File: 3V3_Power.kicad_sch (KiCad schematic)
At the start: 5 parts, among them U5 AP2127N-3.3TRG1

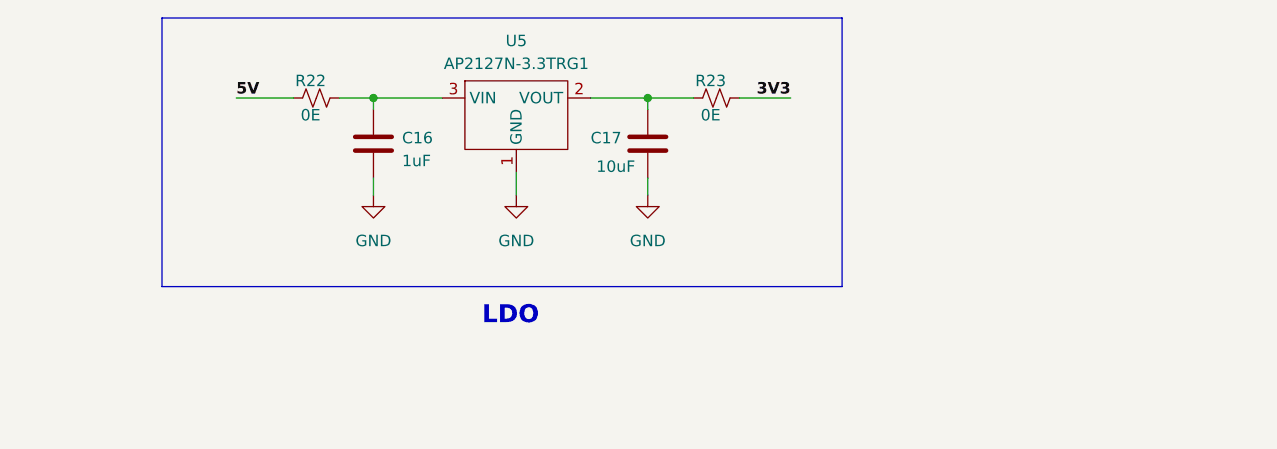
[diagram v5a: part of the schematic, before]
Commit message: Added bulk Decoupling and arranged components
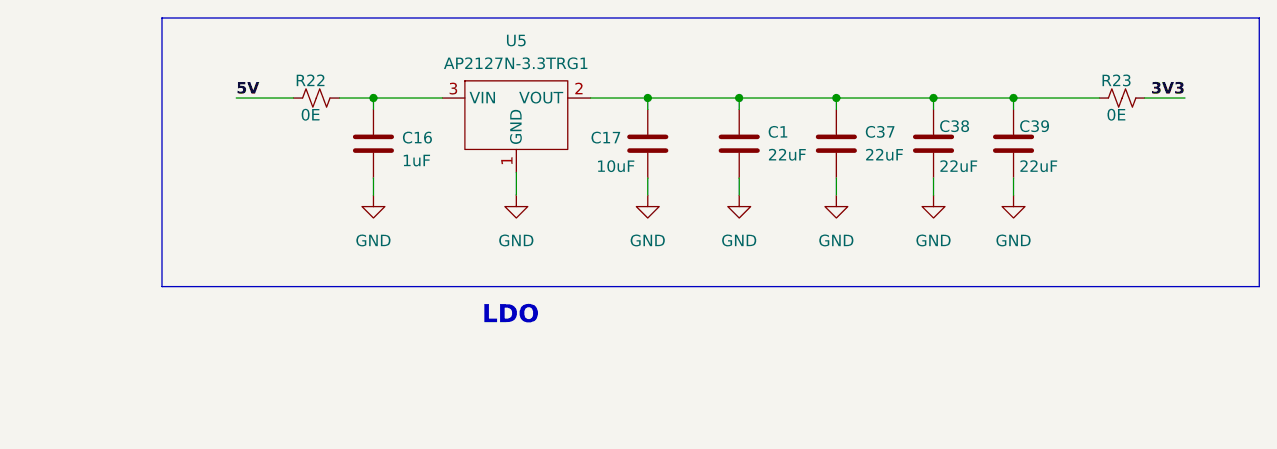
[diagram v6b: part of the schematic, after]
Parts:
- added C1, C37, C38, C39: 22uF, ESP32-S3_Dev_Board:C_1206_3216Metric, symbol ESP32-S3_DB:C
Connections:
- net GND: now also C1.2, C37.2, C38.2, C39.2
- net at C17.1, R23.1, U5.2 (VOUT): now also C1.1, C37.1, C38.1, C39.1
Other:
- moved on the sheet: R23

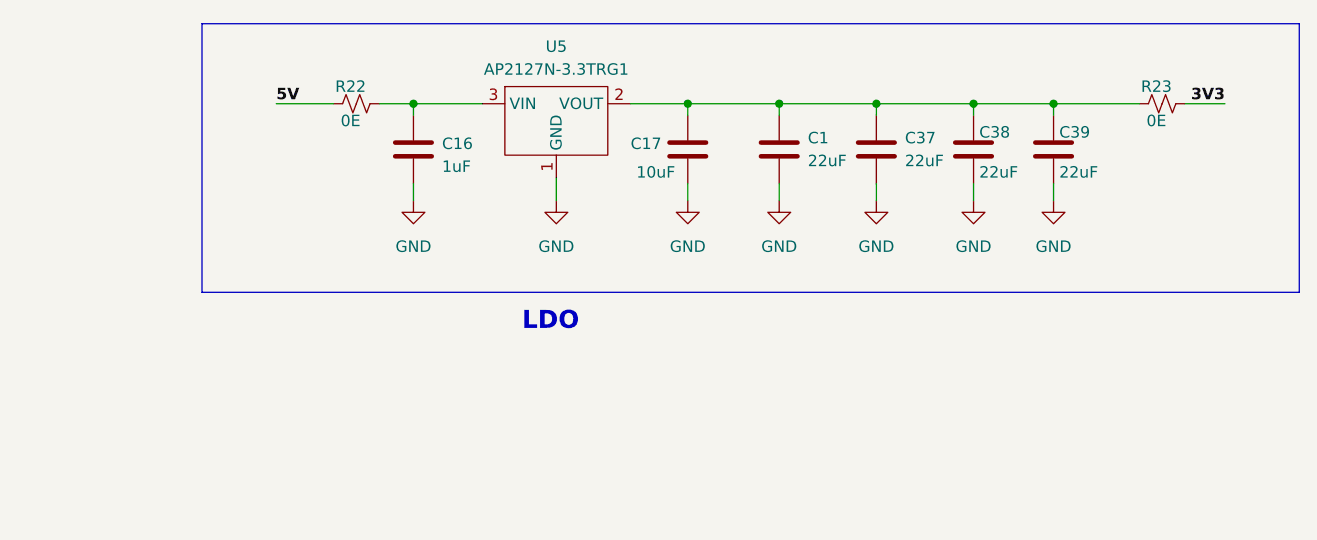
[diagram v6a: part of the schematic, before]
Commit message: Corrected schematic to PCB export error and warings and IP5306 and SD card section
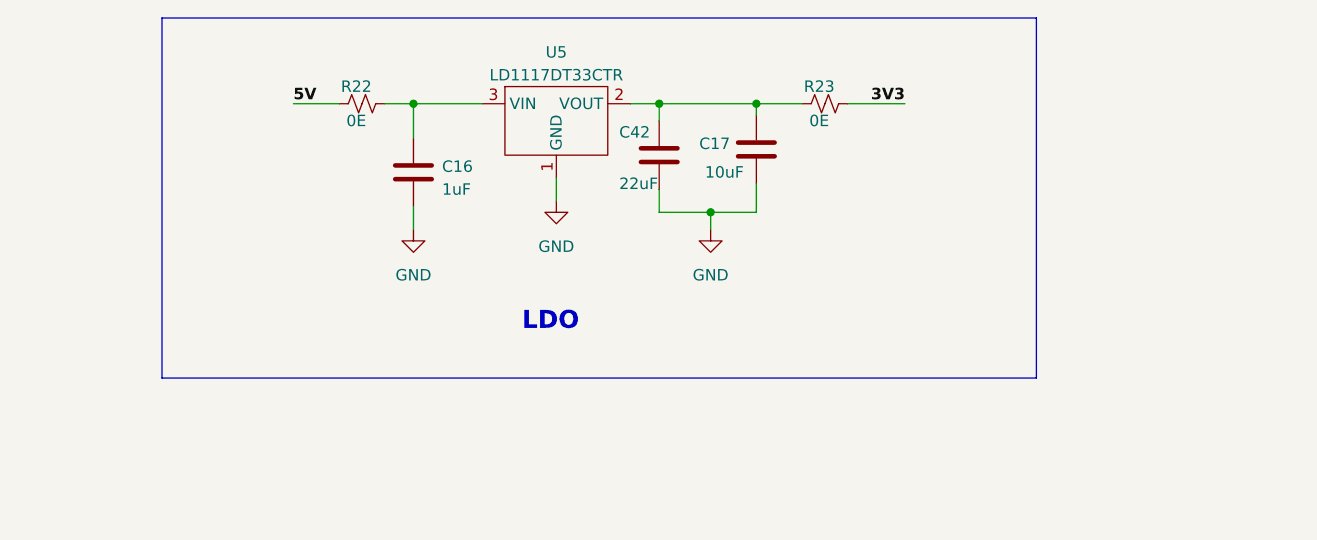
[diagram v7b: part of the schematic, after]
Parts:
- removed C1, C37, C38, C39: 22uF, ESP32-S3_Dev_Board:C_1206_3216Metric, symbol ESP32-S3_DB:C
- added C42: 22uF, ESP32-S3_Dev_Board:C_1206_3216Metric, symbol ESP32-S3_DB:C
- U5: value AP2127N-3.3TRG1 -> LD1117DT33CTR; footprint ESP32-S3_Dev_Board:SOT-23-3 -> ESP32-S3_Dev_Board:DPAK; PN AP2127N-3.3TRG1 -> LD1117DT33CTR
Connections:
- net GND: now also C42.2
- net at C17.1, R23.1, U5.2 (VOUT): now also C42.1
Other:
- moved on the sheet: C16, C17, R22, R23

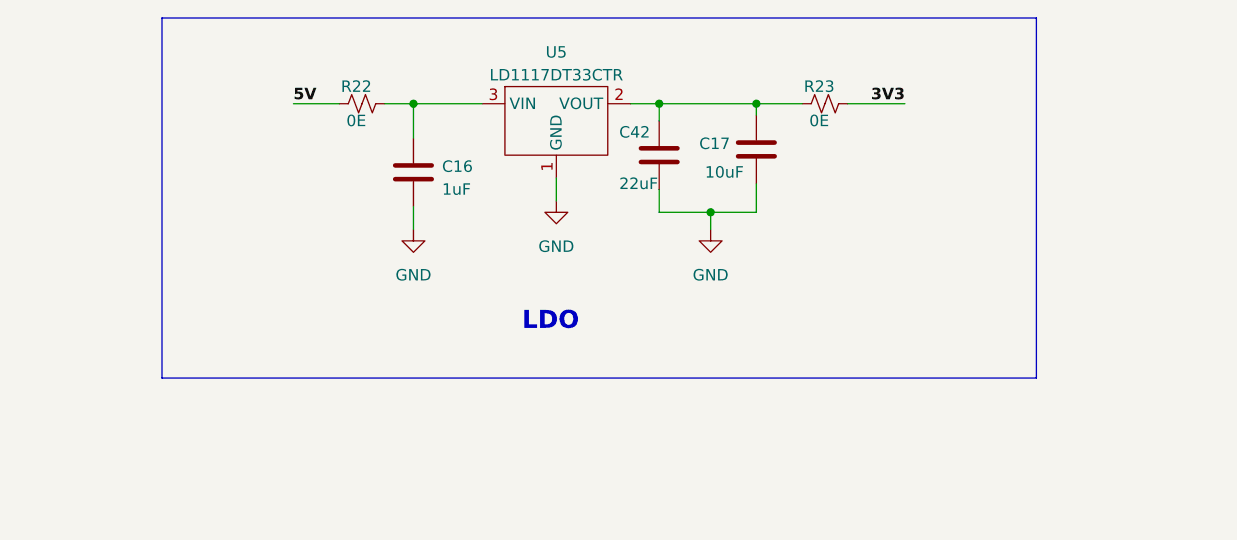
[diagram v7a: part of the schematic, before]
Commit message: Corrected RS485 schematic
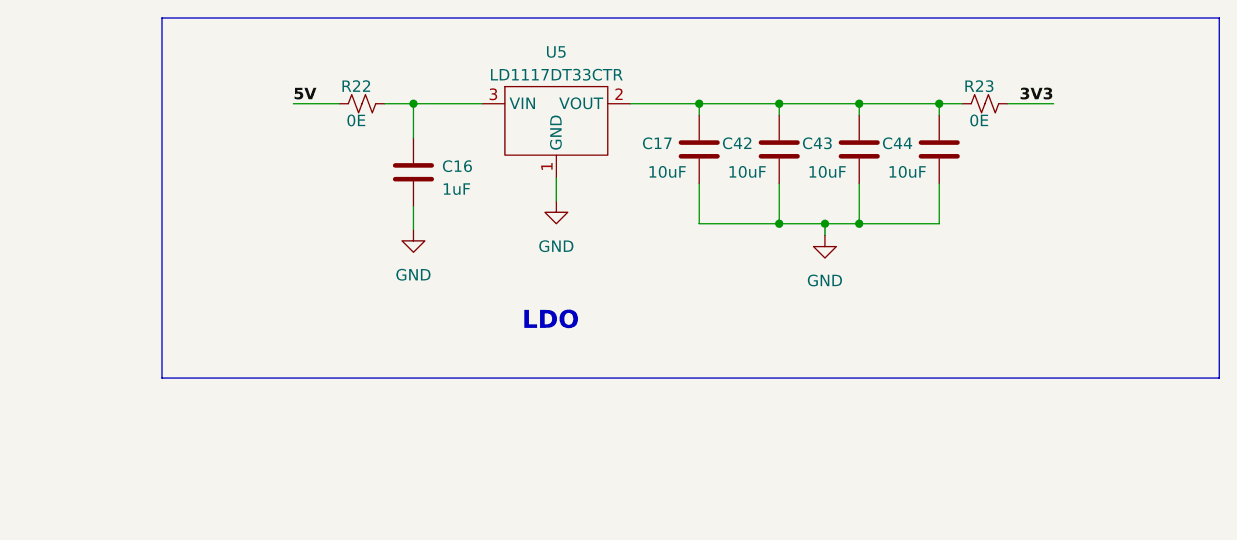
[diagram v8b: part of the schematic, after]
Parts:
- added C43, C44: 10uF, ESP32-S3_Dev_Board:C_0805_2012Metric, symbol ESP32-S3_DB:C
- C42: value 22uF -> 10uF; footprint ESP32-S3_Dev_Board:C_1206_3216Metric -> ESP32-S3_Dev_Board:C_0805_2012Metric; PN CL31A226KAHNNNE -> CL21A106KAYNNNE
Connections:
- net GND: now also C43.2, C44.2
- net at C17.1, C42.1, R23.1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: now also C43.1, C44.1
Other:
- moved on the sheet: C17, R23
